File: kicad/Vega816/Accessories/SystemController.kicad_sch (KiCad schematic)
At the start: 3 parts, among them J102 VIA Port

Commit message: system controller
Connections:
- net GND: now also U?.4 (E1), U?.5 (E2), U?.8 (GND)
- net PA0 renamed ~{EEPROM_WR_1}
- net PA1 renamed ~{EEPROM_RD_1}
- net PA2 renamed ~{EEPROM_WR_0}
- net PA3 renamed ~{EEPROM_RD_0}
- net PA4 renamed B_DMA_PRIORITY
- net PA5 renamed B_RDY_IN
- net PA6 renamed ~{B_CLK_SLOW}
- net PA7 renamed ~{A_CLK_SLOW}
- net PB6 renamed VIA_TIMER2
- net PB7 renamed VIA_TIMER1
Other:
- note added: "PB0 Output SPI_CS0 PB1 Output SPI_CS1 PB2 Output SPI_CS2 PB3 Output SPI_SCK PB4 Output SPI_MOSI PB5 Input SPI_MISO PB6 Input Timer 2 PB7 Output Timer 1"
- note added: "VIA Port Device System Controller / 8 Channel SPI"
- note removed: "PB0 Output SPI_CS0 PB1 Output SPI_CS1 PB2 Output SPI_CS2 PB3 Output SPI_SCK PB4 Output SPI_MOSI PB5 Input SPI_MISO PB6 Reserved PB7 Reserved"
- note removed: "VIA Port Device System Controller"
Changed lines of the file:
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@@
   (junction (at 68.58 99.06) (diameter 0) (color 0 0 0 0)
+  )
+  (junction (at 146.05 119.38) (diameter 0) (color 0 0 0 0)
   )
   (junction (at 212.09 119.38) (diameter 0) (color 0 0 0 0)
@@
     (stroke (width 0) (type default) (color 0 0 0 0))
   )
+  (wire (pts (xy 81.28 119.38) (xy 97.79 119.38))
+    (stroke (width 0) (type default) (color 0 0 0 0))
+  )
   (wire (pts (xy 212.09 123.19) (xy 212.09 124.46))
     (stroke (width 0) (type default) (color 0 0 0 0))
@@
     (stroke (width 0) (type default) (color 0 0 0 0))
   )
+  (wire (pts (xy 81.28 91.44) (xy 96.52 91.44))
+    (stroke (width 0) (type default) (color 0 0 0 0))
+  )
   (wire (pts (xy 154.94 109.22) (xy 154.94 110.49))
     (stroke (width 0) (type default) (color 0 0 0 0))
@@
     (stroke (width 0) (type default) (color 0 0 0 0))
   )
+  (wire (pts (xy 81.28 132.08) (xy 97.79 132.08))
+    (stroke (width 0) (type default) (color 0 0 0 0))
+  )
+  (wire (pts (xy 81.28 129.54) (xy 97.79 129.54))
+    (stroke (width 0) (type default) (color 0 0 0 0))
+  )
   (wire (pts (xy 143.51 101.6) (xy 81.28 101.6))
     (stroke (width 0) (type default) (color 0 0 0 0))
@@
     (stroke (width 0) (type default) (color 0 0 0 0))
   )
+  (wire (pts (xy 81.28 88.9) (xy 96.52 88.9))
+    (stroke (width 0) (type default) (color 0 0 0 0))
+  )
   (wire (pts (xy 140.97 106.68) (xy 81.28 106.68))
     (stroke (width 0) (type default) (color 0 0 0 0))
@@
     (stroke (width 0) (type default) (color 0 0 0 0))
   )
+  (wire (pts (xy 81.28 116.84) (xy 97.79 116.84))
+    (stroke (width 0) (type default) (color 0 0 0 0))
+  )
   (wire (pts (xy 68.58 111.76) (xy 68.58 114.3))
     (stroke (width 0) (type default) (color 0 0 0 0))
@@
     (stroke (width 0) (type default) (color 0 0 0 0))
   )
+  (wire (pts (xy 81.28 121.92) (xy 97.79 121.92))
+    (stroke (width 0) (type default) (color 0 0 0 0))
+  )
   (wire (pts (xy 68.58 124.46) (xy 68.58 127))
     (stroke (width 0) (type default) (color 0 0 0 0))
   )
+  (wire (pts (xy 81.28 114.3) (xy 97.79 114.3))
+    (stroke (width 0) (type default) (color 0 0 0 0))
+  )
   (wire (pts (xy 154.94 114.3) (xy 151.13 114.3))
     (stroke (width 0) (type default) (color 0 0 0 0))
@@
     (stroke (width 0) (type default) (color 0 0 0 0))
   )
+  (wire (pts (xy 81.28 124.46) (xy 97.79 124.46))
+    (stroke (width 0) (type default) (color 0 0 0 0))
+  )
   (wire (pts (xy 180.34 106.68) (xy 199.39 106.68))
     (stroke (width 0) (type default) (color 0 0 0 0))
@@
     (stroke (width 0) (type default) (color 0 0 0 0))
   )
+  (wire (pts (xy 81.28 127) (xy 97.79 127))
+    (stroke (width 0) (type default) (color 0 0 0 0))
+  )
   (wire (pts (xy 68.58 101.6) (xy 68.58 104.14))
     (stroke (width 0) (type default) (color 0 0 0 0))
@@
     (stroke (width 0) (type default) (color 0 0 0 0))
   )
-  (text "PB0 Output SPI_CS0\nPB1 Output SPI_CS1\nPB2 Output SPI_CS2\nPB3 Output SPI_SCK\nPB4 Output SPI_MOSI\nPB5 Input  SPI_MISO\nPB6 Reserved\nPB7 Reserved\n"
+  (text "PB0 Output SPI_CS0\nPB1 Output SPI_CS1\nPB2 Output SPI_CS2\nPB3 Output SPI_SCK\nPB4 Output SPI_MOSI\nPB5 Input  SPI_MISO\nPB6 Input  Timer 2\nPB7 Output Timer 1\n"
     (at 59.69 54.61 0)
     (effects (font (size 1.27 1.27)) (justify left bottom))
   )
   (text "PA0 Output CPU A ~{A_CLK_SLOW} \nPA1 Output CPU B ~{B_CLK_SLOW} \nPA2 Output CPU B B_RDY_IN\nPA3 Output CPU B ~{B_DMA_PRIORITY}\nPA4 Output DMA 0 ~{EEPROM_RD_0}\nPA5 Output DMA 0 EEPROM_WR_0\nPA6 Output DMA 1 ~{EEPROM_RD_1}\nPA7 Output DMA 1 EEPROM_WR_1\n"
-    (at 24.13 54.61 0)
-    (effects (font (size 1.27 1.27)) (justify left bottom))
-  )
-  (text "VIA Port Device\nSystem Controller" (at 16.51 34.29 0)
+    (at 20.32 55.88 0)
+    (effects (font (size 1.27 1.27)) (justify left bottom))
+  )
+  (text "VIA Port Device\nSystem Controller / 8 Channel SPI" (at 16.51 34.29 0)
     (effects (font (size 5 5)) (justify left bottom))
   )
@@
     (effects (font (size 1.27 1.27)) (justify left bottom))
   )
+  (label "SPI_CS1" (at 86.36 104.14 0)
+    (effects (font (size 1.27 1.27)) (justify left bottom))
+  )
+  (label "SPI_MOSI" (at 86.36 96.52 0)
+    (effects (font (size 1.27 1.27)) (justify left bottom))
+  )
   (label "CB2" (at 81.28 83.82 0)
     (effects (font (size 1.27 1.27)) (justify left bottom))
@@
     (effects (font (size 1.27 1.27)) (justify left bottom))
   )
+  (label "SPI_SCK" (at 86.36 99.06 0)
+    (effects (font (size 1.27 1.27)) (justify left bottom))
+  )
   (label "PB6" (at 81.28 91.44 0)
     (effects (font (size 1.27 1.27)) (justify left bottom))
@@
     (effects (font (size 1.27 1.27)) (justify right bottom))
   )
+  (label "SPI_CS2" (at 86.36 101.6 0)
+    (effects (font (size 1.27 1.27)) (justify left bottom))
+  )
   (label "PA4" (at 81.28 121.92 0)
     (effects (font (size 1.27 1.27)) (justify left bottom))
@@
     (effects (font (size 1.27 1.27)) (justify left bottom))
   )
+  (label "SPI_CS0" (at 86.3953 106.68 0)
+    (effects (font (size 1.27 1.27)) (justify left bottom))
+  )
   (label "GND" (at 199.39 124.46 180)
     (effects (font (size 1.27 1.27)) (justify right bottom))
@@
     (effects (font (size 1.27 1.27)) (justify left bottom))
   )
+  (label "SPI_MISO" (at 86.36 93.98 0)
+    (effects (font (size 1.27 1.27)) (justify left bottom))
+  )
   (label "PB4" (at 81.28 96.52 0)
     (effects (font (size 1.27 1.27)) (justify left bottom))
+  )
+  (global_label "B_DMA_PRIORITY" (shape output) (at 97.79 121.92 0) (fields_autoplaced)
+    (effects (font (size 1.27 1.27)) (justify left))
+    (property "Intersheet References" "${INTERSHEET_REFS}" (id 0) (at 115.6245 121.8406 0)
+      (effects (font (size 1.27 1.27)) (justify left) hide)
+    )
+  )
+  (global_label "~{EEPROM_RD_0}" (shape output) (at 97.79 124.46 0) (fields_autoplaced)
+    (effects (font (size 1.27 1.27)) (justify left))
+    (property "Intersheet References" "${INTERSHEET_REFS}" (id 0) (at 113.5079 124.3806 0)
+      (effects (font (size 1.27 1.27)) (justify left) hide)
+    )
+  )
+  (global_label "VIA_TIMER2" (shape input) (at 96.52 91.44 0) (fields_autoplaced)
+    (effects (font (size 1.27 1.27)) (justify left))
+    (property "Intersheet References" "${INTERSHEET_REFS}" (id 0) (at 109.335 91.3606 0)
+      (effects (font (size 1.27 1.27)) (justify left) hide)
+    )
+  )
+  (global_label "~{B_CLK_SLOW}" (shape output) (at 97.79 116.84 0) (fields_autoplaced)
+    (effects (font (size 1.27 1.27)) (justify left))
+    (property "Intersheet References" "${INTERSHEET_REFS}" (id 0) (at 111.996 116.7606 0)
+      (effects (font (size 1.27 1.27)) (justify left) hide)
+    )
+  )
+  (global_label "~{A_CLK_SLOW}" (shape output) (at 97.79 114.3 0) (fields_autoplaced)
+    (effects (font (size 1.27 1.27)) (justify left))
+    (property "Intersheet References" "${INTERSHEET_REFS}" (id 0) (at 111.8145 114.2206 0)
+      (effects (font (size 1.27 1.27)) (justify left) hide)
+    )
+  )
+  (global_label "~{EEPROM_RD_1}" (shape output) (at 97.79 129.54 0) (fields_autoplaced)
+    (effects (font (size 1.27 1.27)) (justify left))
+    (property "Intersheet References" "${INTERSHEET_REFS}" (id 0) (at 113.5079 129.4606 0)
+      (effects (font (size 1.27 1.27)) (justify left) hide)
+    )
+  )
+  (global_label "B_RDY_IN" (shape output) (at 97.79 119.38 0) (fields_autoplaced)
+    (effects (font (size 1.27 1.27)) (justify left))
+    (property "Intersheet References" "${INTERSHEET_REFS}" (id 0) (at 108.9721 119.3006 0)
+      (effects (font (size 1.27 1.27)) (justify left) hide)
+    )
+  )
+  (global_label "~{EEPROM_WR_1}" (shape output) (at 97.79 132.08 0) (fields_autoplaced)
+    (effects (font (size 1.27 1.27)) (justify left))
+    (property "Intersheet References" "${INTERSHEET_REFS}" (id 0) (at 113.6893 132.0006 0)
+      (effects (font (size 1.27 1.27)) (justify left) hide)
+    )
+  )
+  (global_label "~{EEPROM_WR_0}" (shape output) (at 97.79 127 0) (fields_autoplaced)
+    (effects (font (size 1.27 1.27)) (justify left))
+    (property "Intersheet References" "${INTERSHEET_REFS}" (id 0) (at 113.6893 126.9206 0)
+      (effects (font (size 1.27 1.27)) (justify left) hide)
+    )
+  )
+  (global_label "VIA_TIMER1" (shape output) (at 96.52 88.9 0) (fields_autoplaced)
+    (effects (font (size 1.27 1.27)) (justify left))
+    (property "Intersheet References" "${INTERSHEET_REFS}" (id 0) (at 109.335 88.8206 0)
+      (effects (font (size 1.27 1.27)) (justify left) hide)
+    )
   )
   (symbol (lib_id "Vega816:74ACH138") (at 167.64 109.22 0) (unit 1)
@@
       (effects (font (size 1.27 1.27)) hide)
     )
+    (pin "1")
+  )
+  (symbol (lib_name "GND_2") (lib_id "power:GND") (at 146.05 119.38 0) (unit 1)
+    (in_bom yes) (on_board yes)
+    (property "Reference" "#PWR?" (id 0) (at 146.05 125.73 0)
+      (effects (font (size 1.27 1.27)) hide)
+    )
+    (property "Value" "GND" (id 1) (at 146.05 123.19 0))
+    (property "Footprint" "" (id 2) (at 146.05 119.38 0)
+      (effects (font (size 1.27 1.27)) hide)
+    )
+    (property "Datasheet" "" (id 3) (at 146.05 119.38 0)
+      (effects (font (size 1.27 1.27)) hide)
+    )

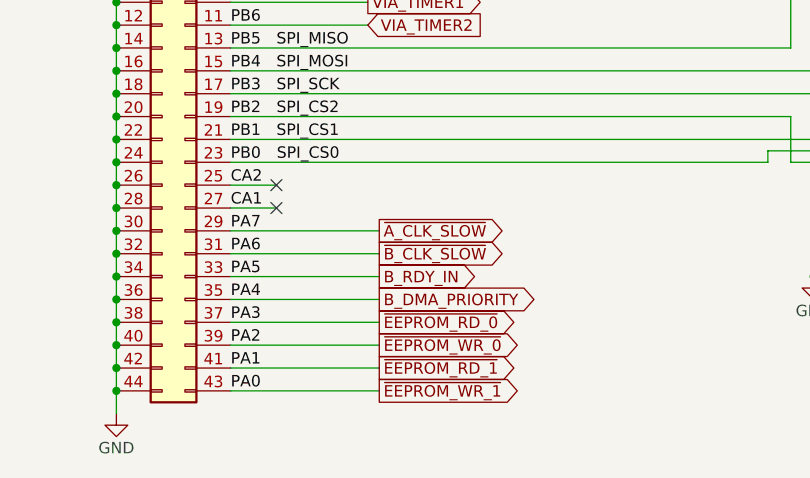
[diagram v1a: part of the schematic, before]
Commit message: via port rework
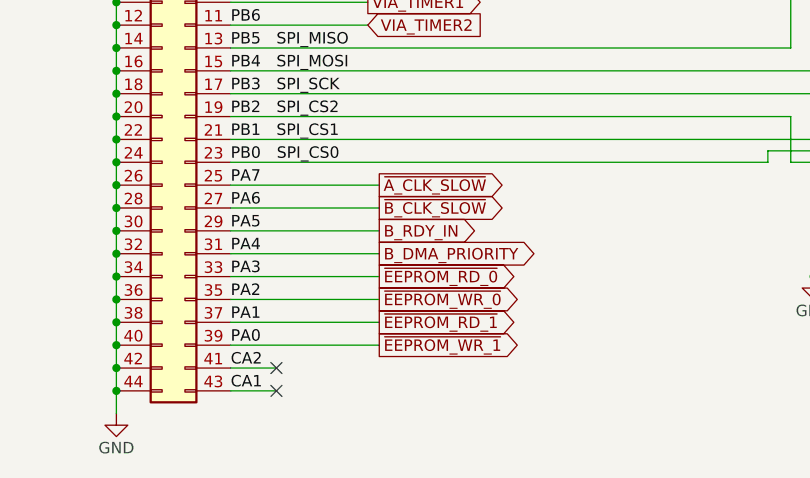
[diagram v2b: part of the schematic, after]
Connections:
- net B_DMA_PRIORITY: now also J102.31 (Pin_31); no longer J102.35 (Pin_35)
- net B_RDY_IN: now also J102.29 (Pin_29); no longer J102.33 (Pin_33)
- net CA1: now also J102.43 (Pin_43); no longer J102.27 (Pin_27)
- net CA2: now also J102.41 (Pin_41); no longer J102.25 (Pin_25)
- net ~{A_CLK_SLOW}: now also J102.25 (Pin_25); no longer J102.29 (Pin_29)
- net ~{B_CLK_SLOW}: now also J102.27 (Pin_27); no longer J102.31 (Pin_31)
- net ~{EEPROM_RD_0}: now also J102.33 (Pin_33); no longer J102.37 (Pin_37)
- net ~{EEPROM_RD_1}: now also J102.37 (Pin_37); no longer J102.41 (Pin_41)
- net ~{EEPROM_WR_0}: now also J102.35 (Pin_35); no longer J102.39 (Pin_39)
- net ~{EEPROM_WR_1}: now also J102.39 (Pin_39); no longer J102.43 (Pin_43)

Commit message: expansion port hi ram
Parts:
- added R? (x8): 10K, symbol Device:R
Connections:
- net B_DMA_PRIORITY: now also R?.1
- net B_RDY_IN: now also R?.1
- net GND: now also R?.2, R?.2, R?.2, R?.2, R?.2, R?.2, R?.2, R?.2
- net ~{A_CLK_SLOW}: now also R?.1
- net ~{B_CLK_SLOW}: now also R?.1
- net ~{EEPROM_RD_0}: now also R?.1
- net ~{EEPROM_RD_1}: now also R?.1
- net ~{EEPROM_WR_0} renamed EEPROM_WR_0
- net EEPROM_WR_0: now also R?.1
- net ~{EEPROM_WR_1} renamed EEPROM_WR_1
- net EEPROM_WR_1: now also R?.1
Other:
- note added: "On ~{RES}, PA is set to inputs with bus holding devices. Pulldown resistors pull all System Controls low. Write $00 to PA before changing PA DDR to output."

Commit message: new plots
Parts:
- removed J?: SPI, symbol Connector_Generic:Conn_02x13_Odd_Even
- removed U?: 74ACH138, symbol Vega816:74ACH138
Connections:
- net B_DMA_PRIORITY renamed ~{B_DMA_PRIORITY}
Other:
- note added: "VIA Port Device System Controller"
- note removed: "VIA Port Device System Controller / 8 Channel SPI"

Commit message: Big push, Sysctl, DMA Reg
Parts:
- removed R? (x8): 10K, symbol Device:R
- added J1: Sysctrl $7, Connector_PinHeader_2.54mm:PinHeader_2x08_P2.54mm_Vertical, symbol Vega816:Conn_02x08_Odd_Even
- added J10: Sysctrl $A, Connector_PinHeader_2.54mm:PinHeader_2x08_P2.54mm_Vertical, symbol Vega816:Conn_02x08_Odd_Even
- added J11: Sysctrl $B, Connector_PinHeader_2.54mm:PinHeader_2x08_P2.54mm_Vertical, symbol Vega816:Conn_02x08_Odd_Even
- added J12: Sysctrl $C, Connector_PinHeader_2.54mm:PinHeader_2x08_P2.54mm_Vertical, symbol Vega816:Conn_02x08_Odd_Even
- added J13: Sysctrl $D, Connector_PinHeader_2.54mm:PinHeader_2x08_P2.54mm_Vertical, symbol Vega816:Conn_02x08_Odd_Even
- added J16: Sysctrl $E, Connector_PinHeader_2.54mm:PinHeader_2x08_P2.54mm_Vertical, symbol Vega816:Conn_02x08_Odd_Even
- added J17: Sysctrl $F, Connector_PinHeader_2.54mm:PinHeader_2x08_P2.54mm_Vertical, symbol Vega816:Conn_02x08_Odd_Even
- added J18: Sysctrl $8, Connector_PinHeader_2.54mm:PinHeader_2x08_P2.54mm_Vertical, symbol Vega816:Conn_02x08_Odd_Even
- added J2: Sysctrl $6, Connector_PinHeader_2.54mm:PinHeader_2x08_P2.54mm_Vertical, symbol Vega816:Conn_02x08_Odd_Even
- added J3: Sysctrl $5, Connector_PinHeader_2.54mm:PinHeader_2x08_P2.54mm_Vertical, symbol Vega816:Conn_02x08_Odd_Even
- added J4: Sysctrl $4, Connector_PinHeader_2.54mm:PinHeader_2x08_P2.54mm_Vertical, symbol Vega816:Conn_02x08_Odd_Even
- added J5: Sysctrl $3, Connector_PinHeader_2.54mm:PinHeader_2x08_P2.54mm_Vertical, symbol Vega816:Conn_02x08_Odd_Even
- added J6: Sysctrl $2, Connector_PinHeader_2.54mm:PinHeader_2x08_P2.54mm_Vertical, symbol Vega816:Conn_02x08_Odd_Even
- added J7: Sysctrl $1, Connector_PinHeader_2.54mm:PinHeader_2x08_P2.54mm_Vertical, symbol Vega816:Conn_02x08_Odd_Even
- added J8: Sysctrl $0, Connector_PinHeader_2.54mm:PinHeader_2x08_P2.54mm_Vertical, symbol Vega816:Conn_02x08_Odd_Even
- added J9: Sysctrl $9, Connector_PinHeader_2.54mm:PinHeader_2x08_P2.54mm_Vertical, symbol Vega816:Conn_02x08_Odd_Even
- added U11, U18, U22, U32, U49, U53, U57, U6: 74HC32, Package_DIP:DIP-14_W7.62mm_Socket, symbol Vega816:74HC32
- added U15, U20, U30, U47, U5, U51, U55, U59: 74HC259, symbol Vega816:74HC259
- added U17, U48, U60, U63, U67, U70, U73, U?: 74HC373, symbol 74xx:74HC373
- added U2, U3: 74ACH138, Package_DIP:DIP-14_W7.62mm_Socket, symbol Vega816:74ACH138
- added U21, U52, U61, U65, U68, U7, U71, U74: 74HC02, symbol 74xx:74HC02
- added U4: 74HC04, symbol 74xx:74HC04
- added U? (x16): 74HC541, symbol Vega816:74HC541
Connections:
- net GND: now also J10.10 (Pin_10), J10.12 (Pin_12), J10.14 (Pin_14), J10.16 (Pin_16), J10.2 (Pin_2), J10.4 (Pin_4), J10.6 (Pin_6), J10.8 (Pin_8), J11.10 (Pin_10), J11.12 (Pin_12), J11.14 (Pin_14), J11.16 (Pin_16), J11.2 (Pin_2), J11.4 (Pin_4), J11.6 (Pin_6), J11.8 (Pin_8), J12.10 (Pin_10), J12.12 (Pin_12), J12.14 (Pin_14), J12.16 (Pin_16), J12.2 (Pin_2), J12.4 (Pin_4), J12.6 (Pin_6), J12.8 (Pin_8), J13.10 (Pin_10), J13.12 (Pin_12), J13.14 (Pin_14), J13.16 (Pin_16), J13.2 (Pin_2), J13.4 (Pin_4), J13.6 (Pin_6), J13.8 (Pin_8), J16.10 (Pin_10), J16.12 (Pin_12), J16.14 (Pin_14), J16.16 (Pin_16), J16.2 (Pin_2), J16.4 (Pin_4), J16.6 (Pin_6), J16.8 (Pin_8), J17.10 (Pin_10), J17.12 (Pin_12), J17.14 (Pin_14), J17.16 (Pin_16), J17.2 (Pin_2), J17.4 (Pin_4), J17.6 (Pin_6), J17.8 (Pin_8), J18.10 (Pin_10), J18.12 (Pin_12), J18.14 (Pin_14), J18.16 (Pin_16), J18.2 (Pin_2), J18.4 (Pin_4), J18.6 (Pin_6), J18.8 (Pin_8), J4.10 (Pin_10), J4.12 (Pin_12), J4.14 (Pin_14), J4.16 (Pin_16), J4.2 (Pin_2), J4.4 (Pin_4), J4.6 (Pin_6), J4.8 (Pin_8), J8.10 (Pin_10), J8.12 (Pin_12), J8.14 (Pin_14), J8.16 (Pin_16), J8.2 (Pin_2), J8.4 (Pin_4), J8.6 (Pin_6), J8.8 (Pin_8), J9.10 (Pin_10), J9.12 (Pin_12), J9.14 (Pin_14), J9.16 (Pin_16), J9.2 (Pin_2), J9.4 (Pin_4), J9.6 (Pin_6), J9.8 (Pin_8), U15.8 (GND), U17.1 (OE), U17.10 (GND), U20.8 (GND), U30.8 (GND), U47.8 (GND), U48.1 (OE), U48.10 (GND), U5.8 (GND), U51.8 (GND), U55.8 (GND), U59.8 (GND), U60.1 (OE), U60.10 (GND), U63.1 (OE), U63.10 (GND), U67.1 (OE), U67.10 (GND), U70.1 (OE), U70.10 (GND), U73.1 (OE), U73.10 (GND), U?.1 (OE), U?.10 (GND), U?.10 (GND), U?.10 (GND), U?.10 (GND), U?.10 (GND), U?.10 (GND), U?.10 (GND), U?.10 (GND), U?.10 (GND), U?.10 (GND), U?.10 (GND), U?.10 (GND), U?.10 (GND), U?.10 (GND), U?.10 (GND), U?.10 (GND), U?.10 (GND)
- net VCC: now also U15.16 (VCC), U17.20 (VCC), U20.16 (VCC), U30.16 (VCC), U47.16 (VCC), U48.20 (VCC), U5.16 (VCC), U51.16 (VCC), U55.16 (VCC), U59.16 (VCC), U60.20 (VCC), U63.20 (VCC), U67.20 (VCC), U70.20 (VCC), U73.20 (VCC), U?.20 (VCC), U?.20 (VCC), U?.20 (VCC), U?.20 (VCC), U?.20 (VCC), U?.20 (VCC), U?.20 (VCC), U?.20 (VCC), U?.20 (VCC), U?.20 (VCC), U?.20 (VCC), U?.20 (VCC), U?.20 (VCC), U?.20 (VCC), U?.20 (VCC), U?.20 (VCC), U?.20 (VCC)
- net B_RDY_IN renamed PA5
- net PA5: now also U17.14 (D5), U48.14 (D5), U60.14 (D5), U63.14 (D5), U67.14 (D5), U70.14 (D5), U73.14 (D5), U?.13 (Y5), U?.13 (Y5), U?.13 (Y5), U?.13 (Y5), U?.13 (Y5), U?.13 (Y5), U?.13 (Y5), U?.13 (Y5), U?.14 (D5), U?.16 (Y2), U?.16 (Y2), U?.16 (Y2), U?.16 (Y2), U?.16 (Y2), U?.16 (Y2), U?.16 (Y2), U?.16 (Y2)
- net CA2 renamed CA2_~{LE}
- net CA2_~{LE}: now also U11.1, U21.3, U52.3, U6.1, U61.3, U65.3, U68.3, U7.3, U71.3, U74.3
- net CB2 renamed CB2_CLR
- net CB2_CLR: now also U15.15 (Clr), U20.15 (Clr), U30.15 (Clr), U47.15 (Clr), U5.15 (Clr), U51.15 (Clr), U55.15 (Clr), U59.15 (Clr)
- net EEPROM_WR_0 renamed PA2
- net PA2: now also U17.7 (D2), U48.7 (D2), U60.7 (D2), U63.7 (D2), U67.7 (D2), U70.7 (D2), U73.7 (D2), U?.13 (Y5), U?.13 (Y5), U?.13 (Y5), U?.13 (Y5), U?.13 (Y5), U?.13 (Y5), U?.13 (Y5), U?.13 (Y5), U?.16 (Y2), U?.16 (Y2), U?.16 (Y2), U?.16 (Y2), U?.16 (Y2), U?.16 (Y2), U?.16 (Y2), U?.16 (Y2), U?.7 (D2)
- net EEPROM_WR_1 renamed PA0_D
- net PA0_D: now also U15.13 (D), U17.3 (D0), U20.13 (D), U30.13 (D), U47.13 (D), U48.3 (D0), U5.13 (D), U51.13 (D), U55.13 (D), U59.13 (D), U60.3 (D0), U63.3 (D0), U67.3 (D0), U70.3 (D0), U73.3 (D0), U?.11 (Y7), U?.11 (Y7), U?.11 (Y7), U?.11 (Y7), U?.11 (Y7), U?.11 (Y7), U?.11 (Y7), U?.11 (Y7), U?.18 (Y0), U?.18 (Y0), U?.18 (Y0), U?.18 (Y0), U?.18 (Y0), U?.18 (Y0), U?.18 (Y0), U?.18 (Y0), U?.3 (D0)
- net PB0 renamed PB0_A0
- net PB0_A0: now also U15.1 (A0), U20.1 (A0), U30.1 (A0), U47.1 (A0), U5.1 (A0), U51.1 (A0), U55.1 (A0), U59.1 (A0)
- net PB1 renamed PB1_A1
- net PB1_A1: now also U15.2 (A1), U20.2 (A1), U30.2 (A1), U47.2 (A1), U5.2 (A1), U51.2 (A1), U55.2 (A1), U59.2 (A1)
- net PB2 renamed PB2_A2
- net PB2_A2: now also U15.3 (A2), U20.3 (A2), U30.3 (A2), U47.3 (A2), U5.3 (A2), U51.3 (A2), U55.3 (A2), U59.3 (A2)
- net PB3 renamed PB3_A3
- net PB3_A3: now also U2.1 (A0), U3.1 (A0)
- net PB4 renamed PB4_A4
- net PB4_A4: now also U2.2 (A1), U3.2 (A1)
- net PB5 renamed PB5_A5
- net PB5_A5: now also U2.3 (A2), U3.3 (A2)
- net VIA_TIMER1 renamed PB7_RD
- net PB7_RD: now also U4.1
- net VIA_TIMER2 renamed PB6_A6
- net PB6_A6: now also U2.4 (E1), U3.6 (E3)
- net ~{A_CLK_SLOW} renamed PA7
- net PA7: now also U17.18 (D7), U48.18 (D7), U60.18 (D7), U63.18 (D7), U67.18 (D7), U70.18 (D7), U73.18 (D7), U?.11 (Y7), U?.11 (Y7), U?.11 (Y7), U?.11 (Y7), U?.11 (Y7), U?.11 (Y7), U?.11 (Y7), U?.11 (Y7), U?.18 (D7), U?.18 (Y0), U?.18 (Y0), U?.18 (Y0), U?.18 (Y0), U?.18 (Y0), U?.18 (Y0), U?.18 (Y0), U?.18 (Y0)
- net ~{B_CLK_SLOW} renamed PA6
- net PA6: now also U17.17 (D6), U48.17 (D6), U60.17 (D6), U63.17 (D6), U67.17 (D6), U70.17 (D6), U73.17 (D6), U?.12 (Y6), U?.12 (Y6), U?.12 (Y6), U?.12 (Y6), U?.12 (Y6), U?.12 (Y6), U?.12 (Y6), U?.12 (Y6), U?.17 (D6), U?.17 (Y1), U?.17 (Y1), U?.17 (Y1), U?.17 (Y1), U?.17 (Y1), U?.17 (Y1), U?.17 (Y1), U?.17 (Y1)
- net ~{B_DMA_PRIORITY} renamed PA4
- net PA4: now also U17.13 (D4), U48.13 (D4), U60.13 (D4), U63.13 (D4), U67.13 (D4), U70.13 (D4), U73.13 (D4), U?.13 (D4), U?.14 (Y4), U?.14 (Y4), U?.14 (Y4), U?.14 (Y4), U?.14 (Y4), U?.14 (Y4), U?.14 (Y4), U?.14 (Y4), U?.15 (Y3), U?.15 (Y3), U?.15 (Y3), U?.15 (Y3), U?.15 (Y3), U?.15 (Y3), U?.15 (Y3), U?.15 (Y3)
- net ~{EEPROM_RD_0} renamed PA3
- net PA3: now also U17.8 (D3), U48.8 (D3), U60.8 (D3), U63.8 (D3), U67.8 (D3), U70.8 (D3), U73.8 (D3), U?.14 (Y4), U?.14 (Y4), U?.14 (Y4), U?.14 (Y4), U?.14 (Y4), U?.14 (Y4), U?.14 (Y4), U?.14 (Y4), U?.15 (Y3), U?.15 (Y3), U?.15 (Y3), U?.15 (Y3), U?.15 (Y3), U?.15 (Y3), U?.15 (Y3), U?.15 (Y3), U?.8 (D3)
- net ~{EEPROM_RD_1} renamed PA1
- net PA1: now also U17.4 (D1), U48.4 (D1), U60.4 (D1), U63.4 (D1), U67.4 (D1), U70.4 (D1), U73.4 (D1), U?.12 (Y6), U?.12 (Y6), U?.12 (Y6), U?.12 (Y6), U?.12 (Y6), U?.12 (Y6), U?.12 (Y6), U?.12 (Y6), U?.17 (Y1), U?.17 (Y1), U?.17 (Y1), U?.17 (Y1), U?.17 (Y1), U?.17 (Y1), U?.17 (Y1), U?.17 (Y1), U?.4 (D1)
- new net: J5.1 (Pin_1), U47.12 (Q7)
- new net: J5.10 (Pin_10), U?.5 (A3)
- new net: J5.11 (Pin_11), U47.6 (Q2)
- new net: J5.12 (Pin_12), U?.4 (A2)
- new net: J5.13 (Pin_13), U47.5 (Q1)
- new net: J5.14 (Pin_14), U?.3 (A1)
- new net: J5.15 (Pin_15), U47.4 (Q0)
- new net: J5.16 (Pin_16), U?.2 (A0)
- new net: J5.2 (Pin_2), U?.9 (A7)
- new net: J5.3 (Pin_3), U47.11 (Q6)
- new net: J5.4 (Pin_4), U?.8 (A6)
- new net: J5.5 (Pin_5), U47.10 (Q5)
- new net: J5.6 (Pin_6), U?.7 (A5)
- new net: J5.7 (Pin_7), U47.9 (Q4)
- new net: J5.8 (Pin_8), U?.6 (A4)
- new net: J5.9 (Pin_9), U47.7 (Q3)
- new net: U2.14 (O1), U53.2, U?.1 (G1)
- new net: U4.2, U?.19 (G2), U?.19 (G2), U?.19 (G2), U?.19 (G2), U?.19 (G2), U?.19 (G2), U?.19 (G2), U?.19 (G2), U?.19 (G2), U?.19 (G2), U?.19 (G2), U?.19 (G2), U?.19 (G2), U?.19 (G2), U?.19 (G2), U?.19 (G2)
- new net: J7.16 (Pin_16), U?.2 (A0)
- new net: J7.14 (Pin_14), U?.3 (A1)
- new net: J7.12 (Pin_12), U?.4 (A2)
- new net: J7.10 (Pin_10), U?.5 (A3)
- new net: J7.8 (Pin_8), U?.6 (A4)
- new net: J7.6 (Pin_6), U?.7 (A5)
- new net: J7.4 (Pin_4), U?.8 (A6)
- new net: J7.2 (Pin_2), U?.9 (A7)
- new net: U3.15 (O0), U7.2, U?.1 (G1)
- new net: J18.1 (Pin_1), U?.2 (A0), U?.2 (O0)
- new net: J18.3 (Pin_3), U?.3 (A1), U?.5 (O1)
- new net: J18.5 (Pin_5), U?.4 (A2), U?.6 (O2)
- new net: J18.7 (Pin_7), U?.5 (A3), U?.9 (O3)
- new net: J18.9 (Pin_9), U?.12 (O4), U?.6 (A4)
- new net: J18.11 (Pin_11), U?.15 (O5), U?.7 (A5)
- new net: J18.13 (Pin_13), U?.16 (O6), U?.8 (A6)
- new net: J18.15 (Pin_15), U?.19 (O7), U?.9 (A7)
- new net: U60.11 (LE), U61.1
- new net: J11.9 (Pin_9), U60.12 (O4), U?.6 (A4)
- new net: J11.11 (Pin_11), U60.15 (O5), U?.7 (A5)
- new net: J11.13 (Pin_13), U60.16 (O6), U?.8 (A6)
- new net: J11.15 (Pin_15), U60.19 (O7), U?.9 (A7)
- new net: J11.1 (Pin_1), U60.2 (O0), U?.2 (A0)
- new net: J11.3 (Pin_3), U60.5 (O1), U?.3 (A1)
- new net: J11.5 (Pin_5), U60.6 (O2), U?.4 (A2)
- new net: J11.7 (Pin_7), U60.9 (O3), U?.5 (A3)
- new net: U11.2, U2.9 (O6), U?.1 (G1)
- new net: U11.3, U15.14 (E)
- new net: U17.11 (LE), U21.1
- new net: J9.9 (Pin_9), U17.12 (O4), U?.6 (A4)
- new net: J9.11 (Pin_11), U17.15 (O5), U?.7 (A5)
- new net: J9.13 (Pin_13), U17.16 (O6), U?.8 (A6)
- new net: J9.15 (Pin_15), U17.19 (O7), U?.9 (A7)
- new net: J9.1 (Pin_1), U17.2 (O0), U?.2 (A0)
- new net: J9.3 (Pin_3), U17.5 (O1), U?.3 (A1)
- new net: J9.5 (Pin_5), U17.6 (O2), U?.4 (A2)
- new net: J9.7 (Pin_7), U17.9 (O3), U?.5 (A3)
- new net: U18.2, U2.10 (O5), U?.1 (G1)
- new net: U2.11 (O4), U22.2, U?.1 (G1)
- new net: U2.12 (O3), U32.2, U?.1 (G1)
- new net: U2.13 (O2), U49.2, U?.1 (G1)
- new net: U2.15 (O0), U57.2, U?.1 (G1)
- new net: U2.16 (VCC), U2.6 (E3)
- new net: U2.5 (E2), U2.8 (GND)
- new net: U2.7 (O7), U6.2, U?.1 (G1)
- new net: J7.1 (Pin_1), U55.12 (Q7)
- new net: J7.11 (Pin_11), U55.6 (Q2)
- new net: J7.13 (Pin_13), U55.5 (Q1)
- new net: J7.15 (Pin_15), U55.4 (Q0)
- new net: J7.3 (Pin_3), U55.11 (Q6)
- new net: J7.5 (Pin_5), U55.10 (Q5)
- new net: J7.7 (Pin_7), U55.9 (Q4)
- new net: J7.9 (Pin_9), U55.7 (Q3)
- new net: U18.1, U22.1, U32.1, U49.1
- new net: U22.3, U30.14 (E)
- new net: U3.10 (O5), U68.2, U?.1 (G1)
- new net: J13.1 (Pin_1), U67.2 (O0), U?.2 (A0)
- new net: J13.3 (Pin_3), U67.5 (O1), U?.3 (A1)
- new net: J13.5 (Pin_5), U67.6 (O2), U?.4 (A2)
- new net: J13.7 (Pin_7), U67.9 (O3), U?.5 (A3)
- new net: J13.9 (Pin_9), U67.12 (O4), U?.6 (A4)
- new net: J13.11 (Pin_11), U67.15 (O5), U?.7 (A5)
- new net: J13.13 (Pin_13), U67.16 (O6), U?.8 (A6)
- new net: J13.15 (Pin_15), U67.19 (O7), U?.9 (A7)
- new net: J2.16 (Pin_16), U?.2 (A0)
- new net: J2.14 (Pin_14), U?.3 (A1)
- new net: J2.12 (Pin_12), U?.4 (A2)
- new net: J2.10 (Pin_10), U?.5 (A3)
- new net: J2.8 (Pin_8), U?.6 (A4)
- new net: J2.6 (Pin_6), U?.7 (A5)
- new net: J2.4 (Pin_4), U?.8 (A6)
- new net: J2.2 (Pin_2), U?.9 (A7)
- new net: U21.2, U3.14 (O1), U?.1 (G1)
- new net: J2.5 (Pin_5), U15.10 (Q5)
- new net: J2.3 (Pin_3), U15.11 (Q6)
- new net: J2.1 (Pin_1), U15.12 (Q7)
- new net: J2.15 (Pin_15), U15.4 (Q0)
- new net: J2.13 (Pin_13), U15.5 (Q1)
- new net: J2.11 (Pin_11), U15.6 (Q2)
- new net: J2.9 (Pin_9), U15.7 (Q3)
- new net: J2.7 (Pin_7), U15.9 (Q4)
- new net: U3.12 (O3), U61.2, U?.1 (G1)
- new net: U53.1, U57.1
- new net: U53.3, U55.14 (E)
- new net: J8.15 (Pin_15), U59.4 (Q0), U?.2 (A0)
- new net: J8.13 (Pin_13), U59.5 (Q1), U?.3 (A1)
- new net: J8.11 (Pin_11), U59.6 (Q2), U?.4 (A2)
- new net: J8.9 (Pin_9), U59.7 (Q3), U?.5 (A3)
- new net: J8.7 (Pin_7), U59.9 (Q4), U?.6 (A4)
- new net: J8.5 (Pin_5), U59.10 (Q5), U?.7 (A5)
- new net: J8.3 (Pin_3), U59.11 (Q6), U?.8 (A6)
- new net: J8.1 (Pin_1), U59.12 (Q7), U?.9 (A7)
- new net: U67.11 (LE), U68.1
- new net: U18.3, U20.14 (E)
- new net: U32.3, U47.14 (E)
- new net: U3.9 (O6), U71.2, U?.1 (G1)
- new net: J16.1 (Pin_1), U70.2 (O0), U?.2 (A0)
- new net: J16.3 (Pin_3), U70.5 (O1), U?.3 (A1)
- new net: J16.5 (Pin_5), U70.6 (O2), U?.4 (A2)
- new net: J16.7 (Pin_7), U70.9 (O3), U?.5 (A3)
- new net: J16.9 (Pin_9), U70.12 (O4), U?.6 (A4)
- new net: J16.11 (Pin_11), U70.15 (O5), U?.7 (A5)
- new net: J16.13 (Pin_13), U70.16 (O6), U?.8 (A6)
- new net: J16.15 (Pin_15), U70.19 (O7), U?.9 (A7)
- new net: J12.1 (Pin_1), U63.2 (O0), U?.2 (A0)
- new net: J12.11 (Pin_11), U63.15 (O5), U?.7 (A5)
- new net: J12.13 (Pin_13), U63.16 (O6), U?.8 (A6)
- new net: J12.15 (Pin_15), U63.19 (O7), U?.9 (A7)
- new net: J12.3 (Pin_3), U63.5 (O1), U?.3 (A1)
- new net: J12.5 (Pin_5), U63.6 (O2), U?.4 (A2)
- new net: J12.7 (Pin_7), U63.9 (O3), U?.5 (A3)
- new net: J12.9 (Pin_9), U63.12 (O4), U?.6 (A4)
- new net: J6.1 (Pin_1), U51.12 (Q7)
- new net: J6.10 (Pin_10), U?.5 (A3)
- new net: J6.11 (Pin_11), U51.6 (Q2)
- new net: J6.12 (Pin_12), U?.4 (A2)
- new net: J6.13 (Pin_13), U51.5 (Q1)
- new net: J6.14 (Pin_14), U?.3 (A1)
- new net: J6.15 (Pin_15), U51.4 (Q0)
- new net: J6.16 (Pin_16), U?.2 (A0)
- new net: J6.2 (Pin_2), U?.9 (A7)
- new net: J6.3 (Pin_3), U51.11 (Q6)
- new net: J6.4 (Pin_4), U?.8 (A6)
- new net: J6.5 (Pin_5), U51.10 (Q5)
- new net: J6.6 (Pin_6), U?.7 (A5)
- new net: J6.7 (Pin_7), U51.9 (Q4)
- new net: J6.8 (Pin_8), U?.6 (A4)
- new net: J6.9 (Pin_9), U51.7 (Q3)
- new net: J10.1 (Pin_1), U48.2 (O0), U?.2 (A0)
- new net: J10.11 (Pin_11), U48.15 (O5), U?.7 (A5)
- new net: J10.13 (Pin_13), U48.16 (O6), U?.8 (A6)
- new net: J10.15 (Pin_15), U48.19 (O7), U?.9 (A7)
- new net: J10.3 (Pin_3), U48.5 (O1), U?.3 (A1)
- new net: J10.5 (Pin_5), U48.6 (O2), U?.4 (A2)
- new net: J10.7 (Pin_7), U48.9 (O3), U?.5 (A3)
- new net: J10.9 (Pin_9), U48.12 (O4), U?.6 (A4)
- new net: J3.1 (Pin_1), U20.12 (Q7)
- new net: J3.10 (Pin_10), U?.5 (A3)
- new net: J3.11 (Pin_11), U20.6 (Q2)
- new net: J3.12 (Pin_12), U?.4 (A2)
- new net: J3.13 (Pin_13), U20.5 (Q1)
- new net: J3.14 (Pin_14), U?.3 (A1)
- new net: J3.15 (Pin_15), U20.4 (Q0)
- new net: J3.16 (Pin_16), U?.2 (A0)
- new net: J3.2 (Pin_2), U?.9 (A7)
- new net: J3.3 (Pin_3), U20.11 (Q6)
- new net: J3.4 (Pin_4), U?.8 (A6)
- new net: J3.5 (Pin_5), U20.10 (Q5)
- new net: J3.6 (Pin_6), U?.7 (A5)
- new net: J3.7 (Pin_7), U20.9 (Q4)
- new net: J3.8 (Pin_8), U?.6 (A4)
- new net: J3.9 (Pin_9), U20.7 (Q3)
- new net: U48.11 (LE), U52.1
- new net: U57.3, U59.14 (E)
- new net: J1.16 (Pin_16), U?.2 (A0)
- new net: J1.14 (Pin_14), U?.3 (A1)
- new net: J1.12 (Pin_12), U?.4 (A2)
- new net: J1.10 (Pin_10), U?.5 (A3)
- new net: J1.8 (Pin_8), U?.6 (A4)
- new net: J1.6 (Pin_6), U?.7 (A5)
- new net: J1.4 (Pin_4), U?.8 (A6)
- new net: J1.2 (Pin_2), U?.9 (A7)
- new net: U7.1, U?.11 (LE)
- new net: J4.1 (Pin_1), U30.12 (Q7), U?.9 (A7)
- new net: J4.11 (Pin_11), U30.6 (Q2), U?.4 (A2)
- new net: J4.13 (Pin_13), U30.5 (Q1), U?.3 (A1)
- new net: J4.15 (Pin_15), U30.4 (Q0), U?.2 (A0)
- new net: J4.3 (Pin_3), U30.11 (Q6), U?.8 (A6)
- new net: J4.5 (Pin_5), U30.10 (Q5), U?.7 (A5)
- new net: J4.7 (Pin_7), U30.9 (Q4), U?.6 (A4)
- new net: J4.9 (Pin_9), U30.7 (Q3), U?.5 (A3)
- new net: U3.11 (O4), U65.2, U?.1 (G1)
- new net: U3.7 (O7), U74.2, U?.1 (G1)
- new net: J17.1 (Pin_1), U73.2 (O0), U?.2 (A0)
- new net: J17.3 (Pin_3), U73.5 (O1), U?.3 (A1)
- new net: J17.5 (Pin_5), U73.6 (O2), U?.4 (A2)
- new net: J17.7 (Pin_7), U73.9 (O3), U?.5 (A3)
- new net: J17.9 (Pin_9), U73.12 (O4), U?.6 (A4)
- new net: J17.11 (Pin_11), U73.15 (O5), U?.7 (A5)
- new net: J17.13 (Pin_13), U73.16 (O6), U?.8 (A6)
- new net: J17.15 (Pin_15), U73.19 (O7), U?.9 (A7)
- new net: U3.13 (O2), U52.2, U?.1 (G1)
- new net: U3.4 (E1), U3.5 (E2), U3.8 (GND)
- new net: U63.11 (LE), U65.1
- new net: J1.1 (Pin_1), U5.12 (Q7)
- new net: J1.11 (Pin_11), U5.6 (Q2)
- new net: J1.13 (Pin_13), U5.5 (Q1)
- new net: J1.15 (Pin_15), U5.4 (Q0)
- new net: J1.3 (Pin_3), U5.11 (Q6)
- new net: J1.5 (Pin_5), U5.10 (Q5)
- new net: J1.7 (Pin_7), U5.9 (Q4)
- new net: J1.9 (Pin_9), U5.7 (Q3)
- new net: U70.11 (LE), U71.1
- new net: U49.3, U51.14 (E)
- new net: U73.11 (LE), U74.1
- new net: U5.14 (E), U6.3
- no-connect marks 4 -> 2
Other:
- note added: "Sysctrl Registers 16 x 8 bit latches (8 addressable) VIA Port Device"
- note removed: "On ~{RES}, PA is set to inputs with bus holding devices. Pulldown resistors pull all System Controls low. Write $00 to PA before changing PA DDR to output."
- note removed: "PA0 Output CPU A ~{A_CLK_SLOW} PA1 Output CPU B ~{B_CLK_SLOW} PA2 Output CPU B B_RDY_IN PA3 Output CPU B ~{B_DMA_PRIORITY} PA4 Output DMA 0 ~{EEPROM_RD_0} PA5 Output DMA 0 EEPROM_WR_0 PA6 Output DMA 1 ~{EEPROM_RD_1} PA7 Output DMA 1 EEPROM_WR_1"
- note removed: "PB0 Output SPI_CS0 PB1 Output SPI_CS1 PB2 Output SPI_CS2 PB3 Output SPI_SCK PB4 Output SPI_MOSI PB5 Input SPI_MISO PB6 Input Timer 2 PB7 Output Timer 1"
- note removed: "VIA Port Device System Controller"
- moved on the sheet: J102

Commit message: dfsg
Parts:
- removed J1: Sysctrl $7, Connector_PinHeader_2.54mm:PinHeader_2x08_P2.54mm_Vertical, symbol Vega816:Conn_02x08_Odd_Even
- removed J10: Sysctrl $A, Connector_PinHeader_2.54mm:PinHeader_2x08_P2.54mm_Vertical, symbol Vega816:Conn_02x08_Odd_Even
- removed J102: VIA Port, symbol Connector_Generic:Conn_02x22_Odd_Even
- removed J11: Sysctrl $B, Connector_PinHeader_2.54mm:PinHeader_2x08_P2.54mm_Vertical, symbol Vega816:Conn_02x08_Odd_Even
- removed J12: Sysctrl $C, Connector_PinHeader_2.54mm:PinHeader_2x08_P2.54mm_Vertical, symbol Vega816:Conn_02x08_Odd_Even
- removed J13: Sysctrl $D, Connector_PinHeader_2.54mm:PinHeader_2x08_P2.54mm_Vertical, symbol Vega816:Conn_02x08_Odd_Even
- removed J16: Sysctrl $E, Connector_PinHeader_2.54mm:PinHeader_2x08_P2.54mm_Vertical, symbol Vega816:Conn_02x08_Odd_Even
- removed J17: Sysctrl $F, Connector_PinHeader_2.54mm:PinHeader_2x08_P2.54mm_Vertical, symbol Vega816:Conn_02x08_Odd_Even
- removed J18: Sysctrl $8, Connector_PinHeader_2.54mm:PinHeader_2x08_P2.54mm_Vertical, symbol Vega816:Conn_02x08_Odd_Even
- removed J2: Sysctrl $6, Connector_PinHeader_2.54mm:PinHeader_2x08_P2.54mm_Vertical, symbol Vega816:Conn_02x08_Odd_Even
- removed J3: Sysctrl $5, Connector_PinHeader_2.54mm:PinHeader_2x08_P2.54mm_Vertical, symbol Vega816:Conn_02x08_Odd_Even
- removed J4: Sysctrl $4, Connector_PinHeader_2.54mm:PinHeader_2x08_P2.54mm_Vertical, symbol Vega816:Conn_02x08_Odd_Even
- removed J5: Sysctrl $3, Connector_PinHeader_2.54mm:PinHeader_2x08_P2.54mm_Vertical, symbol Vega816:Conn_02x08_Odd_Even
- removed J6: Sysctrl $2, Connector_PinHeader_2.54mm:PinHeader_2x08_P2.54mm_Vertical, symbol Vega816:Conn_02x08_Odd_Even
- removed J7: Sysctrl $1, Connector_PinHeader_2.54mm:PinHeader_2x08_P2.54mm_Vertical, symbol Vega816:Conn_02x08_Odd_Even
- removed J8: Sysctrl $0, Connector_PinHeader_2.54mm:PinHeader_2x08_P2.54mm_Vertical, symbol Vega816:Conn_02x08_Odd_Even
- removed J9: Sysctrl $9, Connector_PinHeader_2.54mm:PinHeader_2x08_P2.54mm_Vertical, symbol Vega816:Conn_02x08_Odd_Even
- removed U11, U18, U22, U32, U49, U53, U57, U6: 74HC32, Package_DIP:DIP-14_W7.62mm_Socket, symbol Vega816:74HC32
- removed U15, U20, U30, U47, U5, U51, U55, U59: 74HC259, symbol Vega816:74HC259
- removed U17, U48, U60, U63, U67, U70, U73, U?: 74HC373, symbol 74xx:74HC373
- removed U2, U3: 74ACH138, Package_DIP:DIP-14_W7.62mm_Socket, symbol Vega816:74ACH138
- removed U21, U52, U61, U65, U68, U7, U71, U74: 74HC02, symbol 74xx:74HC02
- removed U4: 74HC04, symbol 74xx:74HC04
- removed U? (x16): 74HC541, symbol Vega816:74HC541
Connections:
- no-connect marks 2 -> 0
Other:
- note removed: "Sysctrl Registers 16 x 8 bit latches (8 addressable) VIA Port Device"
